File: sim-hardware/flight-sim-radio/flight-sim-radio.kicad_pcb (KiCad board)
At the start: 2 copper layers, 176 x 45.2 mm, 22 parts, among them J1 Conn_01x04, J2 Conn_01x03, J4 Conn_01x09, SW2 RS-08 300±150GF, SW3 RotaryEncoder_Switch, SW4 RotaryEncoder_Switch, U1 74LS148, U4 TM1637, U5 TM1637

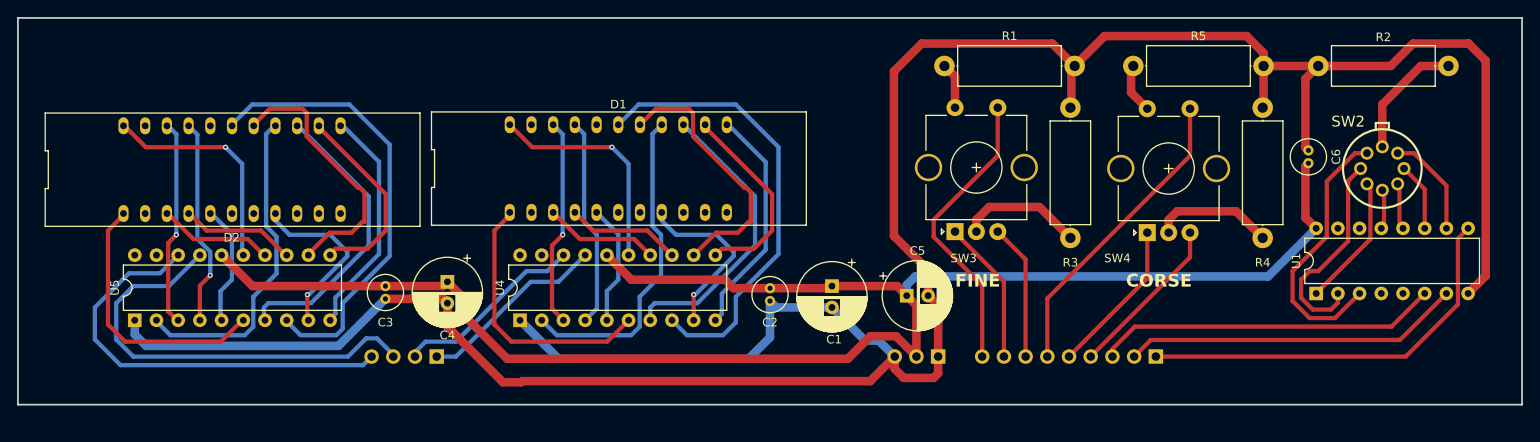
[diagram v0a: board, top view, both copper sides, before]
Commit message: PCB routing updated
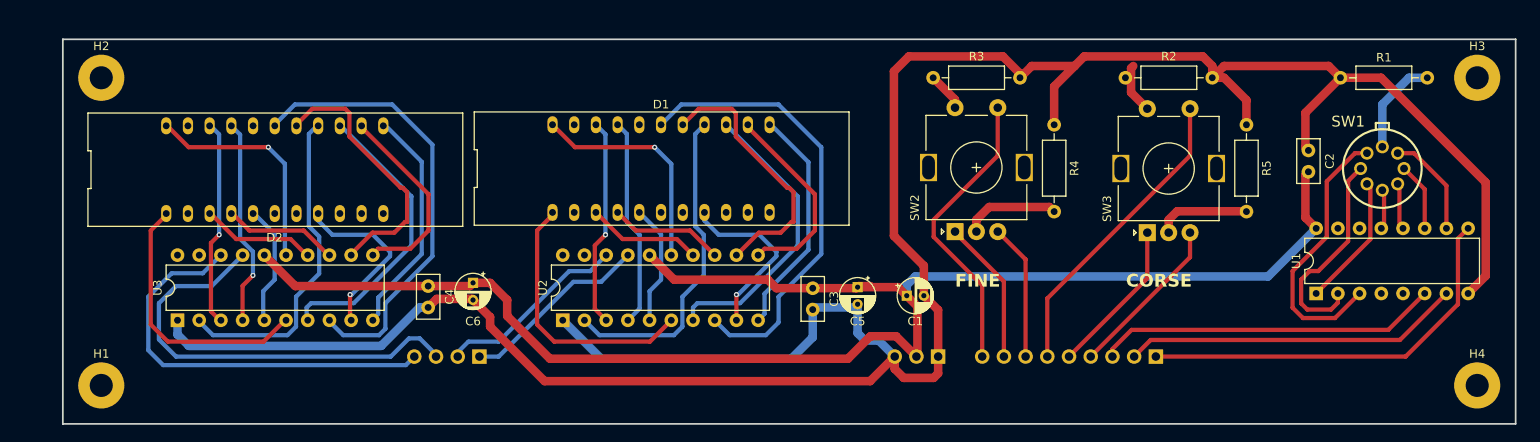
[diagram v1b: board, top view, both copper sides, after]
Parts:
- added H1: MountingHole_Pad, MountingHole:MountingHole_2.7mm_M2.5_Pad, F.Cu at (89.0, 130.5)
- added H2: MountingHole_Pad, MountingHole:MountingHole_2.7mm_M2.5_Pad, F.Cu at (89.0, 94.5)
- added H3: MountingHole_Pad, MountingHole:MountingHole_2.7mm_M2.5_Pad, F.Cu at (250.0, 94.5)
- added H4: MountingHole_Pad, MountingHole:MountingHole_2.7mm_M2.5_Pad, F.Cu at (250.0, 130.5)
- C1: renamed from C5; footprint Capacitor_THT:CP_Radial_D8.0mm_P2.50mm -> Capacitor_THT:CP_Radial_D4.0mm_P2.00mm
- C2: renamed from C6; footprint Capacitor_THT:C_Radial_D4.0mm_H5.0mm_P1.50mm -> Capacitor_THT:C_Disc_D5.0mm_W2.5mm_P2.50mm
- C3: renamed from C2; footprint Capacitor_THT:C_Radial_D4.0mm_H5.0mm_P1.50mm -> Capacitor_THT:C_Disc_D5.0mm_W2.5mm_P2.50mm
- C4: renamed from C3; footprint Capacitor_THT:C_Radial_D4.0mm_H5.0mm_P1.50mm -> Capacitor_THT:C_Disc_D5.0mm_W2.5mm_P2.50mm
- C5: renamed from C1; footprint Capacitor_THT:CP_Radial_D8.0mm_P2.50mm -> Capacitor_THT:CP_Radial_D4.0mm_P2.00mm
- C6: renamed from C4; footprint Capacitor_THT:CP_Radial_D8.0mm_P2.50mm -> Capacitor_THT:CP_Radial_D4.0mm_P2.00mm
- R1: renamed from R2; footprint Resistor_THT:R_Axial_DIN0414_L11.9mm_D4.5mm_P15.24mm_Horizontal -> Resistor_THT:R_Axial_DIN0207_L6.3mm_D2.5mm_P10.16mm_Horizontal
- R2: renamed from R5; footprint Resistor_THT:R_Axial_DIN0414_L11.9mm_D4.5mm_P15.24mm_Horizontal -> Resistor_THT:R_Axial_DIN0207_L6.3mm_D2.5mm_P10.16mm_Horizontal
- R3: renamed from R1; footprint Resistor_THT:R_Axial_DIN0414_L11.9mm_D4.5mm_P15.24mm_Horizontal -> Resistor_THT:R_Axial_DIN0207_L6.3mm_D2.5mm_P10.16mm_Horizontal
- R4: renamed from R3; footprint Resistor_THT:R_Axial_DIN0414_L11.9mm_D4.5mm_P15.24mm_Horizontal -> Resistor_THT:R_Axial_DIN0207_L6.3mm_D2.5mm_P10.16mm_Horizontal
- R5: renamed from R4; footprint Resistor_THT:R_Axial_DIN0414_L11.9mm_D4.5mm_P15.24mm_Horizontal -> Resistor_THT:R_Axial_DIN0207_L6.3mm_D2.5mm_P10.16mm_Horizontal
- SW2: renamed from SW3; footprint Rotary_Encoder:RotaryEncoder_Alps_EC11E-Switch_Vertical_H20mm_CircularMountingHoles -> radio_footprints:ALPSALPINE EC11E09444A8
- SW3: renamed from SW4; footprint Rotary_Encoder:RotaryEncoder_Alps_EC11E-Switch_Vertical_H20mm_CircularMountingHoles -> radio_footprints:ALPSALPINE EC11E09444A8
- moved R3 6.55 mm to (196.5, 94.5)
- moved R2 6.16 mm to (219.0, 94.5)
- moved C3 5.00 mm to (172.2, 119.1)
- moved C4 5.00 mm to (127.2, 118.9)
- moved D1 5.00 mm to (154.5, 105.1)
- moved D2 5.00 mm to (109.3, 105.3)
- moved J3 5.00 mm to (133.2, 127.1)
- moved U2 5.00 mm to (143.0, 122.9)
- moved U3 5.00 mm to (97.9, 122.9)
- moved C5 3.00 mm to (177.5, 119.0)
- moved C6 3.00 mm to (132.5, 118.5)
- moved R1 2.94 mm to (234.0, 94.5)
- moved R4 2.76 mm to (200.5, 100.0)
- moved R5 2.76 mm to (223.0, 100.0)
- renumbered J2 to J1, J4 to J2, J1 to J3, SW2 to SW1, U4 to U2, U5 to U3
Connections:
- net /BUTTON_2 renamed /BUTTON_0
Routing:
- net GND: track 325.1 -> 309.1 mm
- net VDD: track 195.5 -> 185.4 mm
- net Net-(R5-Pad2): track 14.2 -> 11.0 mm
- net Net-(R4-Pad2): track 14.5 -> 11.3 mm
- net Net-(R1-Pad2): track 14.6 -> 11.5 mm
- net Net-(R3-Pad2): track 5.93 -> 4.56 mm
- net /D2_CLK: track 50.1 -> 49.0 mm
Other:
- board size 176 x 45.2 mm -> 170 x 45 mm
- board text added: "+5V"
- board text added: "BT0"
- board text added: "BT1"
- board text added: "D1C"
- board text added: "D1D"
- board text added: "D2C"
- board text added: "D2D"
- board text added: "E0A"
- board text added: "E0B"
- board text added: "E1A"
- board text added: "E1B"
- board text added: "GND"
- board text added: "RS0"
- board text added: "RS1"
- board text added: "RS2"

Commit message: PCB checked
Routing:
- net VDD: track 185.4 -> 183.8 mm
- net Net-(R2-Pad2): track 5.89 -> 4.68 mm
- added copper zone on B.Cu, net GND
- added copper zone on F.Cu, net GND

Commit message: PCB ready for manufacturing
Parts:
- added R6: 10k, Resistor_THT:R_Axial_DIN0207_L6.3mm_D2.5mm_P10.16mm_Horizontal, F.Cu at (136.9, 132.5)
- added R7: 10k, Resistor_THT:R_Axial_DIN0207_L6.3mm_D2.5mm_P10.16mm_Horizontal, F.Cu at (136.9, 129.5)
- added R8: 10k, Resistor_THT:R_Axial_DIN0207_L6.3mm_D2.5mm_P10.16mm_Horizontal, F.Cu at (122.1, 129.5)
- added R9: 10k, Resistor_THT:R_Axial_DIN0207_L6.3mm_D2.5mm_P10.16mm_Horizontal, F.Cu at (122.1, 132.5)
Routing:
- net VDD: track 183.8 -> 246.8 mm
- net /D1_CLK: track 22.6 -> 32.8 mm
- net /D2_DIO: track 51.5 -> 61.7 mm
- net /D1_DIO: track 22.3 -> 27.9 mm
- net /D2_CLK: track 49.0 -> 54.3 mm
- net GND: track 309.4 -> 306.7 mm
- net /D1_SEG5: track 31.4 -> 30.2 mm
